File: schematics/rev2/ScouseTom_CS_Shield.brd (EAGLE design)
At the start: 160 x 54.3 mm, 101 parts, among them IC1 REG1117, IC2 REG1117, IC3 OPA2188AID, U1 AD9954YSVZ, U2 LTC69000, U6 LTC1044CS8PBF, U7 ADUM240D0BRIZ, U8 ADUM240D0BRIZ

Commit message: layout and some polygons done
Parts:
- moved DSUB3 6.35 mm to (4.37, 25.4)
- moved JP5 5.44 mm to (10.2, 25.4)
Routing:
- net IND_START_ISO: track 34.5 -> 25.8 mm
- net IND_STIM_ISO: track 31.8 -> 23.9 mm
- net GND_ISO_TRIG: track 93.0 -> 85.3 mm
- net IND_STOP_ISO: track 29.7 -> 22.2 mm
- net IND_FREQ_ISO: track 37.8 -> 31.4 mm
- net IND_SWITCH_ISO: track 32.8 -> 28.3 mm, vias 1 -> 0
- net IND_EX_2_ISO: track 34.9 -> 38.8 mm
- net IND_EX_3_ISO: track 39.5 -> 43.2 mm
- net IND_EX_1_ISO: track 28.7 -> 31.8 mm
- net +5V: track 142.0 -> 140.2 mm
- net V_ISO_TRIG: track 58.0 -> 59.8 mm
- added copper zone on layer 2, net N$5
- added copper zone on layer 2, net VIN_NEG
- added copper zone on layer 15, net VIN_POS
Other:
- board size 160 x 54.3 mm -> 161.9 x 54.3 mm

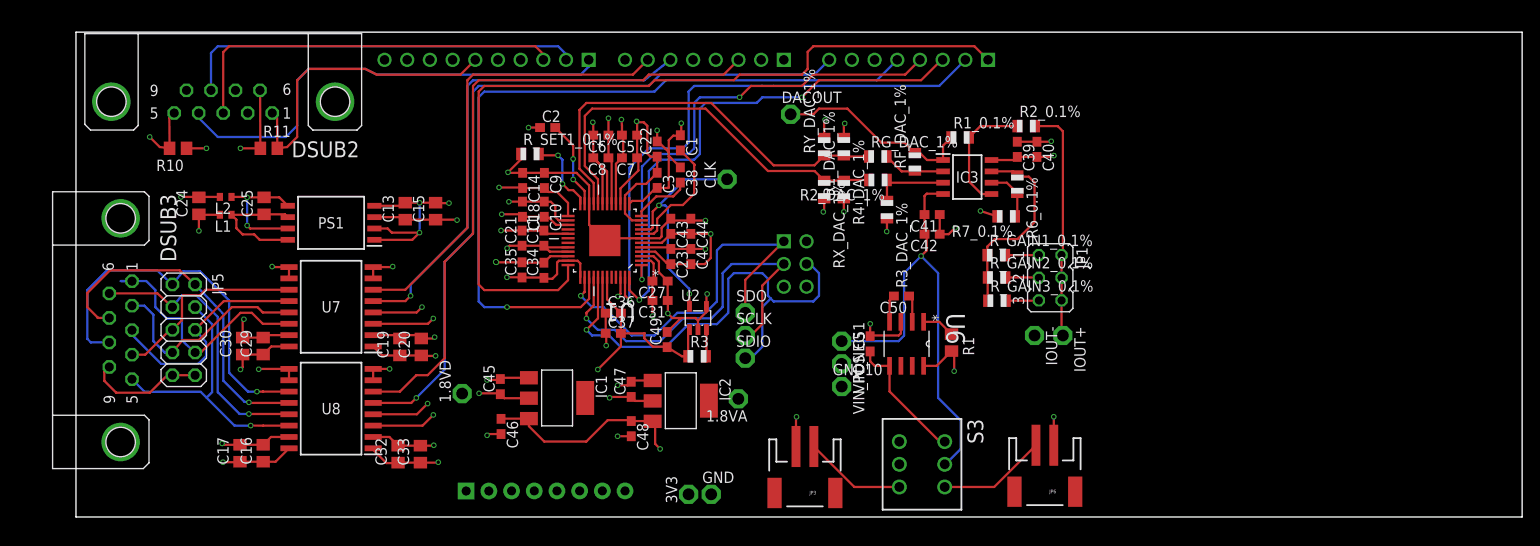
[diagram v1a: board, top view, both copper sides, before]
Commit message: no DRC errors
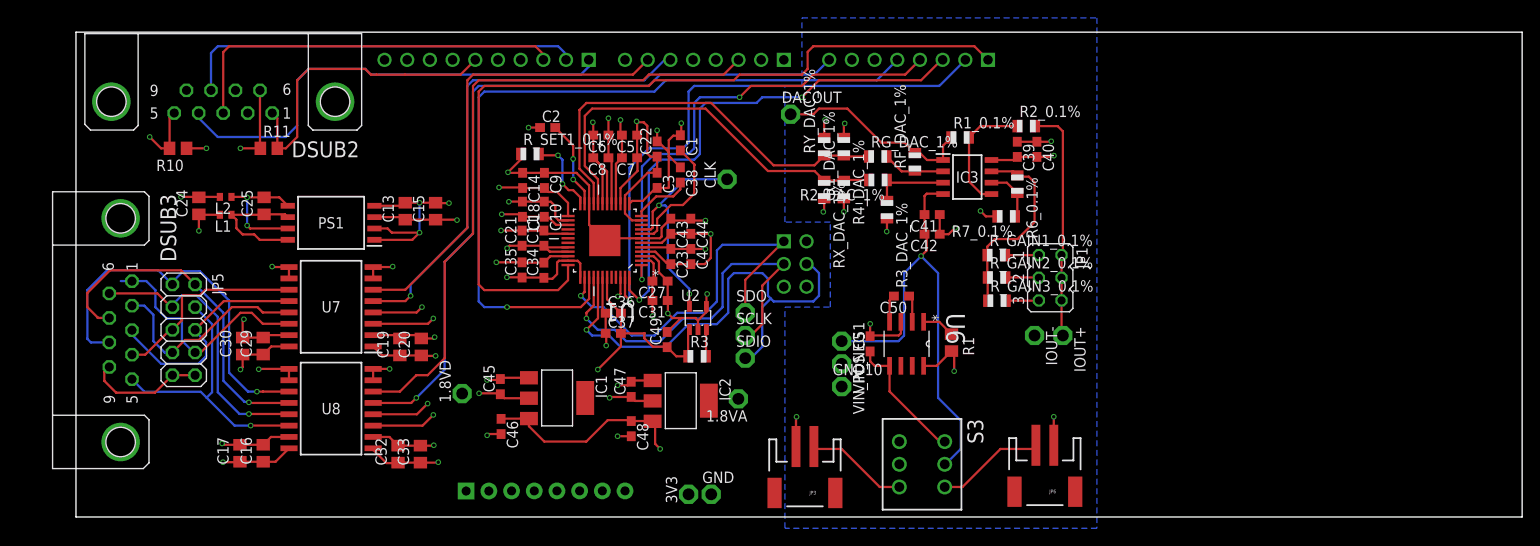
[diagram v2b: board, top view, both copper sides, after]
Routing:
- net GND: track 601.0 -> 599.0 mm
- net IND_SWITCH_ISO: track 28.3 -> 27.1 mm
- net N$13: track 4.16 -> 3.01 mm
- net IND_FREQ: track 91.6 -> 92.3 mm
- net 1V8_ANALOG: track 173.2 -> 172.5 mm
- net A-: track 7.57 -> 7.05 mm
- net 1V8_DIGITAL: track 57.8 -> 57.7 mm, vias 4 -> 3
- added copper zone on layer 16, net VIN_NEG
- removed copper zone on layer 2, net N$5
- removed copper zone on layer 2, net VIN_NEG

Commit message: board finished
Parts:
- added JP2, JP4: (no value), pinhead:1X02
- moved DACOUT 13.4 mm to (91.4, 48.3)
- moved VIN_NEG 3.81 mm to (83.8, 27.9)
- moved GND10 3.81 mm to (83.8, 22.9)
- moved VIN_POS 3.81 mm to (83.8, 25.4)
- renumbered R1_0.1% to R1_H, R1_DAC_1% to R1_DAC, R2_0.1% to R2_H, R2_DAC_1% to R2_DAC, R3_DAC_1% to R3_DAC, R4_DAC_1% to R4_DAC, R6_0.1% to R6_H, R7_0.1% to R7_H, RF_DAC_1% to RF_DAC, RG_DAC_1% to RG_DAC, RX_DAC_1% to RX_DAC, RY_DAC_1% to RY_DAC, R_GAIN1_0.1% to R_HG1, R_GAIN2_0.1% to R_HG2, R_GAIN3_0.1% to R_HG3, R_SET1_0.1% to R_SET1
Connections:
- net GND: now also JP2.2, JP4.1, U$2.GND_5
- net VBAT+: now also JP2.1
- net VBAT-: now also JP4.2
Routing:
- net GND: track 599.0 -> 670.5 mm, vias 35 -> 40
- net GND_ISO_TRIG: track 85.6 -> 153.7 mm, vias 5 -> 14
- net DAC_VOUT: track 22.6 -> 9.68 mm
- net +5V: track 140.2 -> 129.4 mm
- net V_ISO_TRIG: track 59.8 -> 53.1 mm
- net VIN_NEG: track 52.2 -> 45.5 mm
- net SDIO: track 54.2 -> 48.7 mm
- net VBAT+: track 11.4 -> 16.5 mm
- net VBAT-: track 12.1 -> 16.9 mm
- net IND_EX_3: track 72.3 -> 75.3 mm
- net IND_EX_3_ISO: track 43.3 -> 40.7 mm
- net SW_SYNC: track 52.6 -> 50.7 mm
- net 1V8_ANALOG: track 172.5 -> 174.4 mm
- net VIN_POS: track 123.7 -> 125.3 mm
- net SDO: track 44.3 -> 42.8 mm
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- added copper zone on layer 15, net +5V
- added copper zone on layer 1, net GND
- added copper zone on layer 16, net GND
- added copper zone on layer 1, net GND_ISO_TRIG
- added copper zone on layer 16, net GND_ISO_TRIG
- added copper zone on layer 2, net GND_ISO_TRIG
- added copper zone on layer 1, net N$15
- added copper zone on layer 16, net N$16
- added copper zone on layer 2, net N$17
- added copper zone on layer 15, net N$19
- added copper zone on layer 15, net N$5
- added copper zone on layer 1, net N$6
- added copper zone on layer 16, net N$7
- added copper zone on layer 2, net N$8
- added copper zone on layer 15, net N$9
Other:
- board size 161.9 x 54.3 mm -> 114.3 x 54.3 mm
- board text added: "+3V3"
- board text added: "-3V3"
- board text added: "1"
- board text added: "10"
- board text added: "11"
- board text added: "12"
- board text added: "13"
- board text added: "2"
- board text added: "3"
- board text added: "3v3"
- board text added: "4"
- board text added: "5"
- board text added: "5V"
- board text added: "6"
- board text added: "7"
- board text added: "8"
- board text added: "9"
- board text added: "ARD"
- board text added: "BATT"
- board text added: "Batt+"
- board text added: "Batt-"
- board text added: "GND"
- board text added: "HCP PWR SEL"
- board text added: "gnd"

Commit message: Latest Rev2 and USB_ISO
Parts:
- C13, C15, C16, C17, C19, C20, C24, C25, C29, C30, C32, C33: device resistor:C0805 -> resistor:C0603
- IC3: value OPA2188AID -> OPA2188AIDGKR; device OPA2188AID:SOIC127P600X175-8N -> OPA2188AIDGKR:SOP65P490X110-8N
- U2: value LTC69000 -> LTC6900_LTC69000; device LTC6900:SOT23-5L -> Low.Noise.Current.Source:LTC6900_SOT23-5L
- moved IOUT- 0.64 mm to (106.0, 24.8)
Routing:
- net DAC_VOUT: track 9.68 -> 11.9 mm
- net A-: track 7.05 -> 8.51 mm
- net VIN_POS: track 125.3 -> 126.7 mm
- net BOUT: track 22.3 -> 23.4 mm
- net VIN_NEG: track 45.5 -> 46.6 mm
- net A+: track 8.74 -> 9.78 mm
- net B+: track 14.0 -> 13.1 mm
- net B-: track 6.08 -> 6.72 mm
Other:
- board text added: "Current uA 1: 250 2: 100 3: 50"
- board text added: "EEG Triggers"
- board text added: "Switch Network"
